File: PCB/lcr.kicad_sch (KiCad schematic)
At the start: 49 parts, among them J1 Conn_01x04_Pin, J2 Conn_01x04_Pin, J7 USB_C_Receptacle_USB2.0_14P, SW1 SW_Push, SW2 SW_Push, U2 UMW HT7836-A, U5 STM32G431CBT6, U8 TLV757P, U9 USBLC6-2SC6, Y2 8 MHz

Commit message: Fixed some PCB bugs
The OLED display ribbon cable folded the wrong way so the screen faced
down, so I fixed that. Also made vias untented, made diodes
easier to hand solder, and added ground test hook.
The case CAD still needs to be updated.
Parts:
- TP9: footprint TestPoint:TestPoint_Pad_D1.5mm -> TestPoint:TestPoint_Keystone_5000-5004_Miniature
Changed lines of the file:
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@@
 	(title_block
 		(title "LCR Main Section (digital)")
-		(date "2026-05-07")
+		(date "2026-06-03")
 		(company "LWQ")
 	)
@@
 			)
 		)
-		(property "Footprint" "TestPoint:TestPoint_Pad_D1.5mm"
+		(property "Footprint" "TestPoint:TestPoint_Keystone_5000-5004_Miniature"
 			(at 203.2 236.22 0)
 			(hide yes)

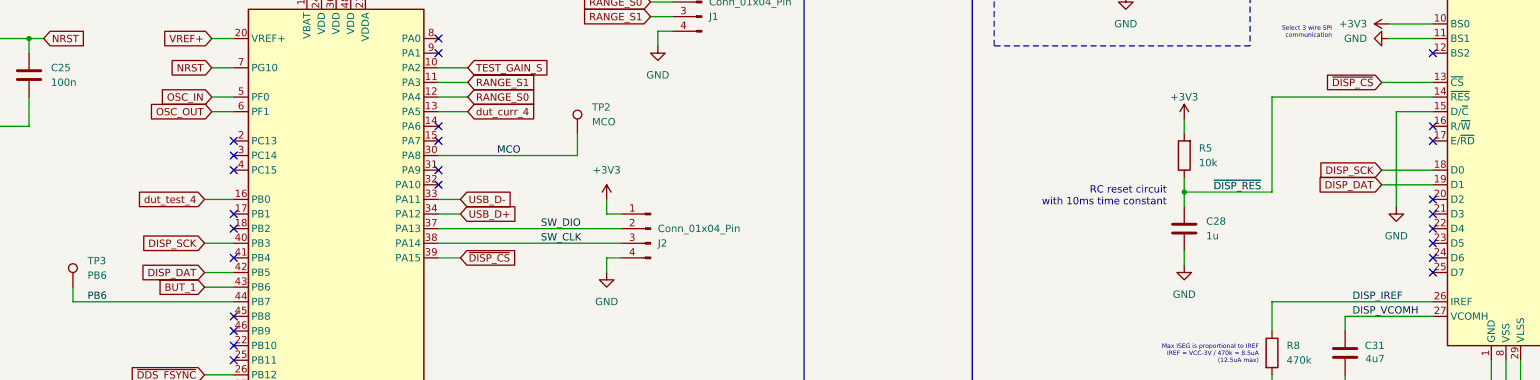
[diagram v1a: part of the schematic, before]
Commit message: Fixed OLED display hardware and code
On the schematic, the OLED pin D2 was left NC, but needed to be tied to
D1. Also the u8g2 SPI code from the last commit was incorrect, as it
didn't use 9-bit SPI mode which is necessary for 3-wire SPI communcation
with the display. I fixed this, and also modified the hardware to allow
4-wire and 3-wire SPI. I'll change the code over to 4-wire when I order
new PCBs.
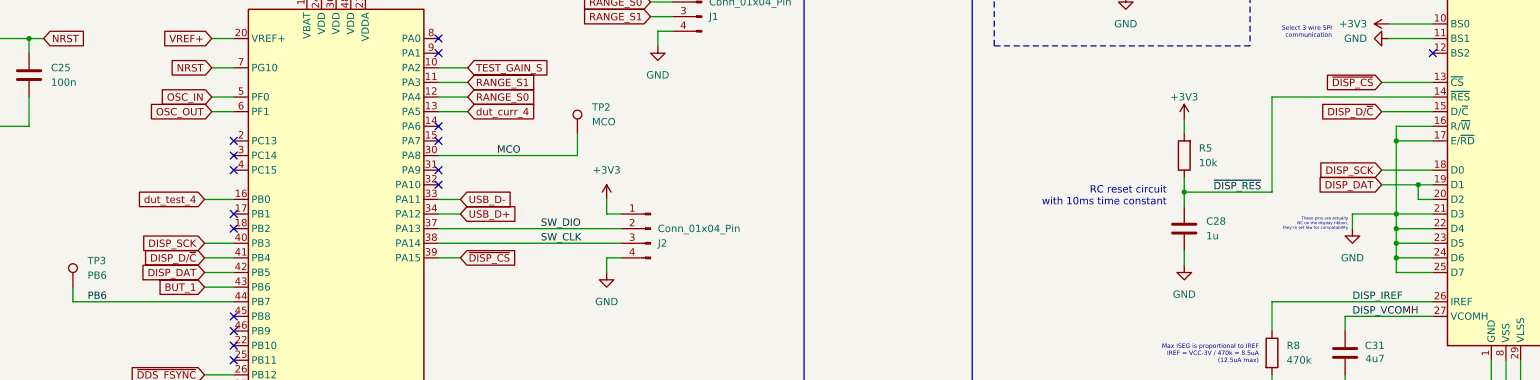
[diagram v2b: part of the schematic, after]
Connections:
- net DISP_DAT: now also DS1.20 (D2)
- net GND: now also DS1.16 (R/~{W}), DS1.17 (E/~{RD}), DS1.21 (D3), DS1.22 (D4), DS1.23 (D5), DS1.24 (D6), DS1.25 (D7); no longer DS1.15 (D/~{C})
- net DISP_D/~{C}: now reaches U5.41 (PB4)
- net DISP_D/~{C}: now also DS1.15 (D/~{C})
- no-connect marks 26 -> 17
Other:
- note added: "These pins are actually NC on the display ribbon, they're set low for compatability"

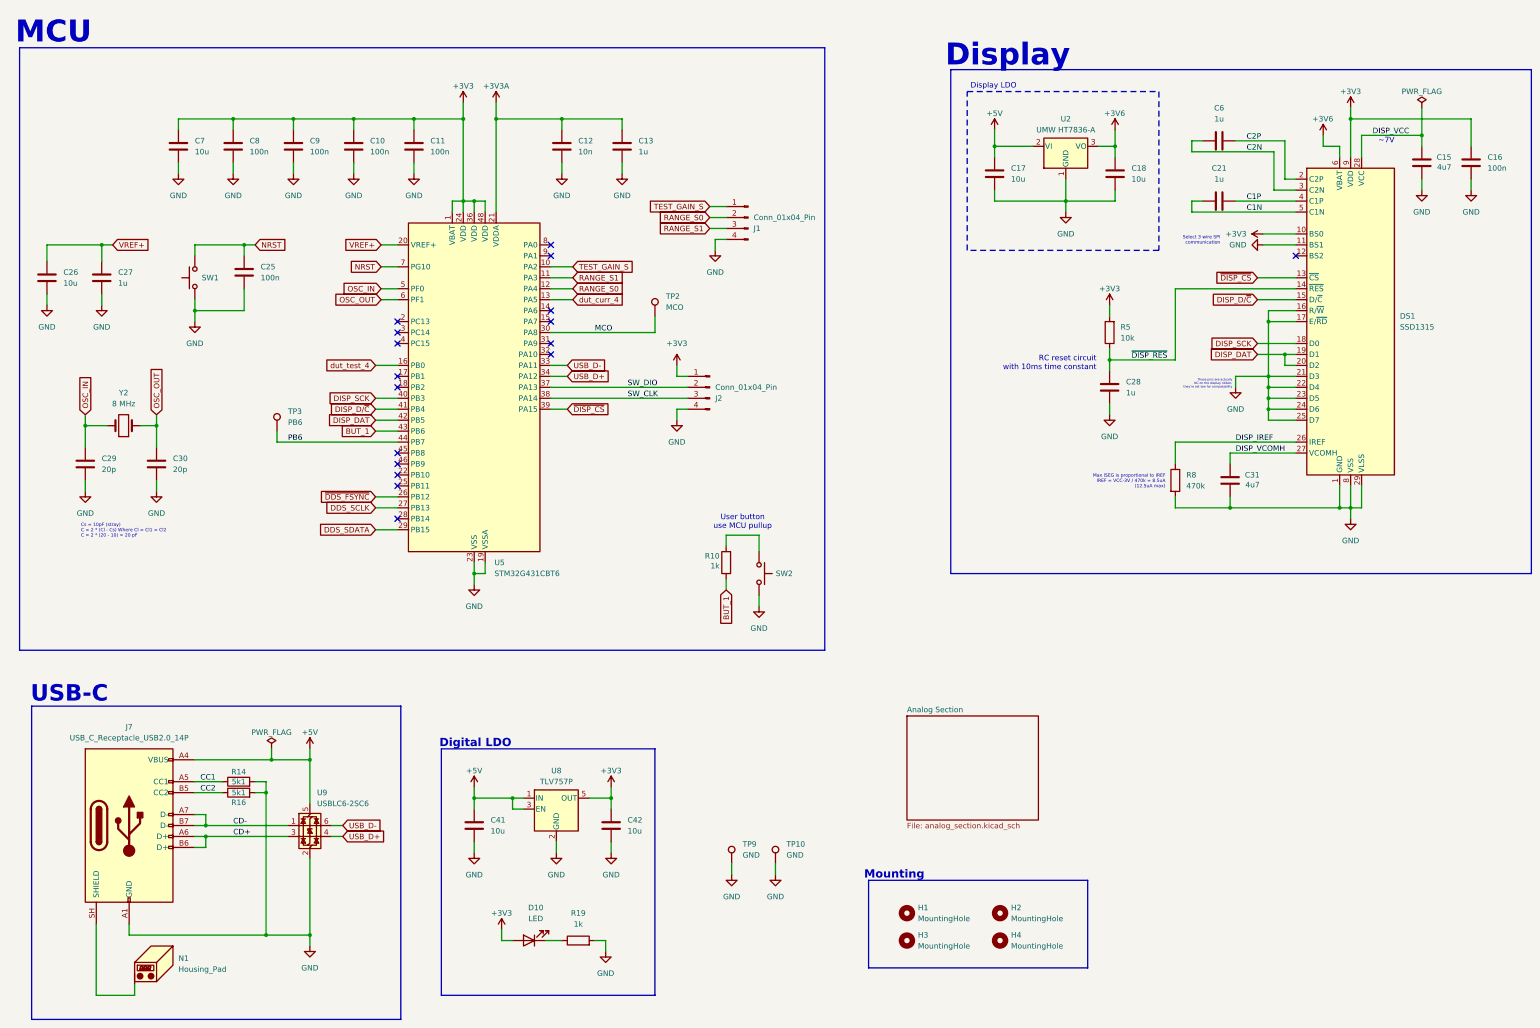
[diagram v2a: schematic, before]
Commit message: Range resistors now use signal relays
Most of the analog section layout was completely overhauled to fit this
change.
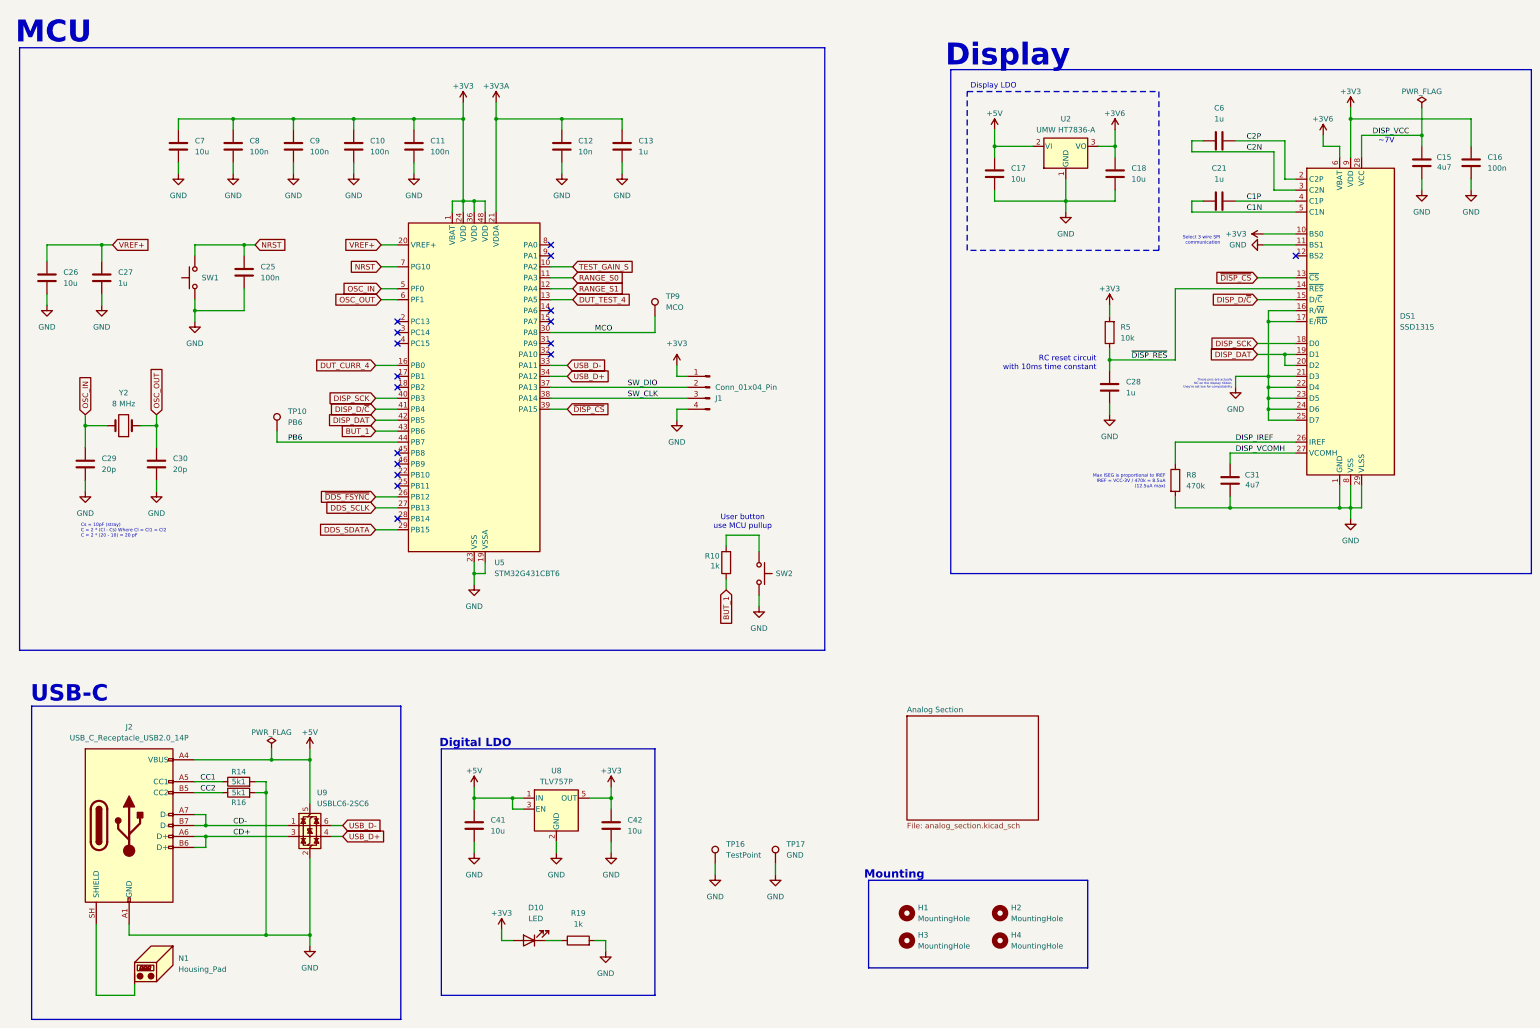
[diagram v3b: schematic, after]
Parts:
- removed J1: Conn_01x04_Pin, Connector_PinHeader_2.54mm:PinHeader_1x04_P2.54mm_Vertical, symbol Connector:Conn_01x04_Pin
- removed TP9: GND, TestPoint:TestPoint_Keystone_5000-5004_Miniature, symbol Connector:TestPoint
- added TP16: TestPoint, TestPoint:TestPoint_Keystone_5000-5004_Miniature, symbol Connector:TestPoint
- renumbered J2 to J1, J7 to J2, TP3 to TP10, TP10 to TP17, TP2 to TP9
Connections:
- net GND: now also TP16.1
- net RANGE_S0: now also U5.11 (PA3); no longer U5.12 (PA4)
- net RANGE_S1: now also U5.12 (PA4); no longer U5.11 (PA3)
- net dut_curr_4 renamed DUT_TEST_4
- net dut_test_4 renamed DUT_CURR_4
